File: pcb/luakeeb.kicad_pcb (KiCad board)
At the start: 2 copper layers, 138.9 x 95.2 mm, 123 parts, among them J1 Pimoroni, SW1 SW_Push, SW10 SW_Push, SW11 SW_Push, SW12 SW_Push, SW13 SW_Push, SW14 SW_Push, SW15 SW_Push, SW16 SW_Push, SW2 SW_Push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

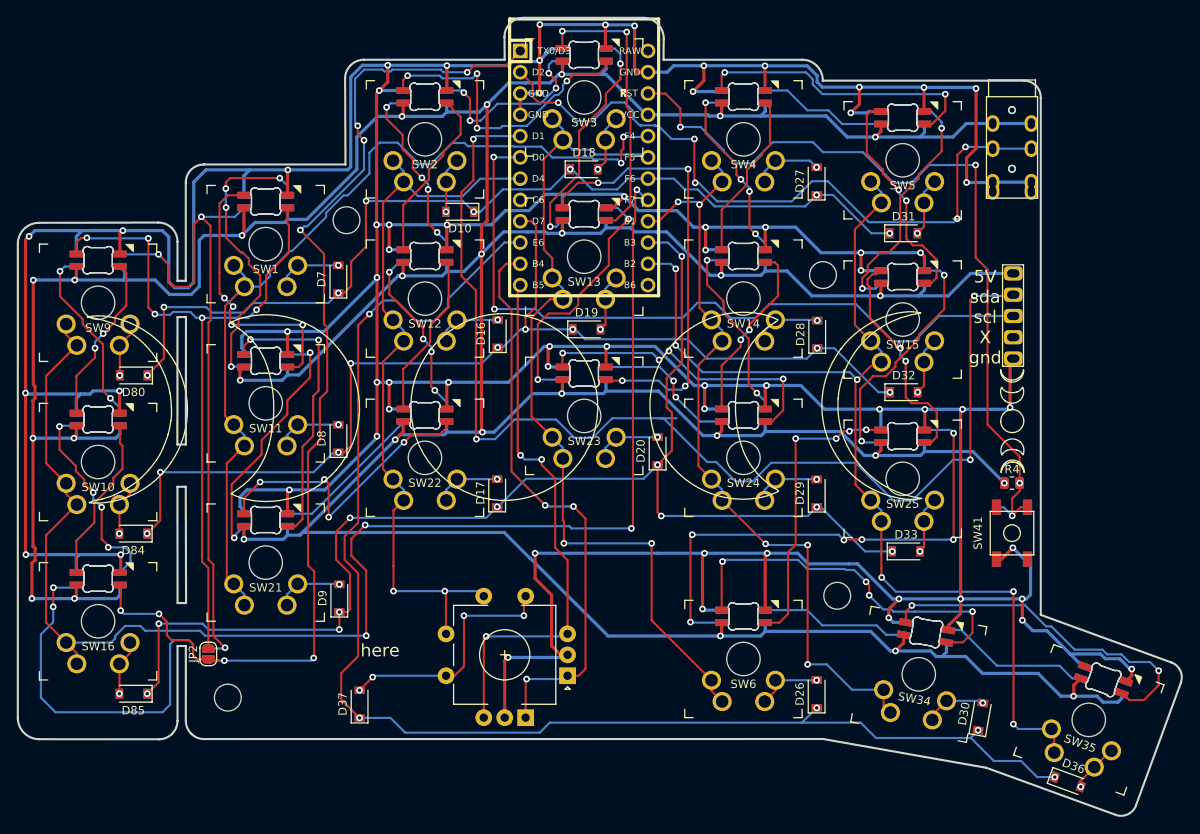
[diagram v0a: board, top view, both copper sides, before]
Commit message: removed the need for separate firmware per half by updating the footprint for the MX switch
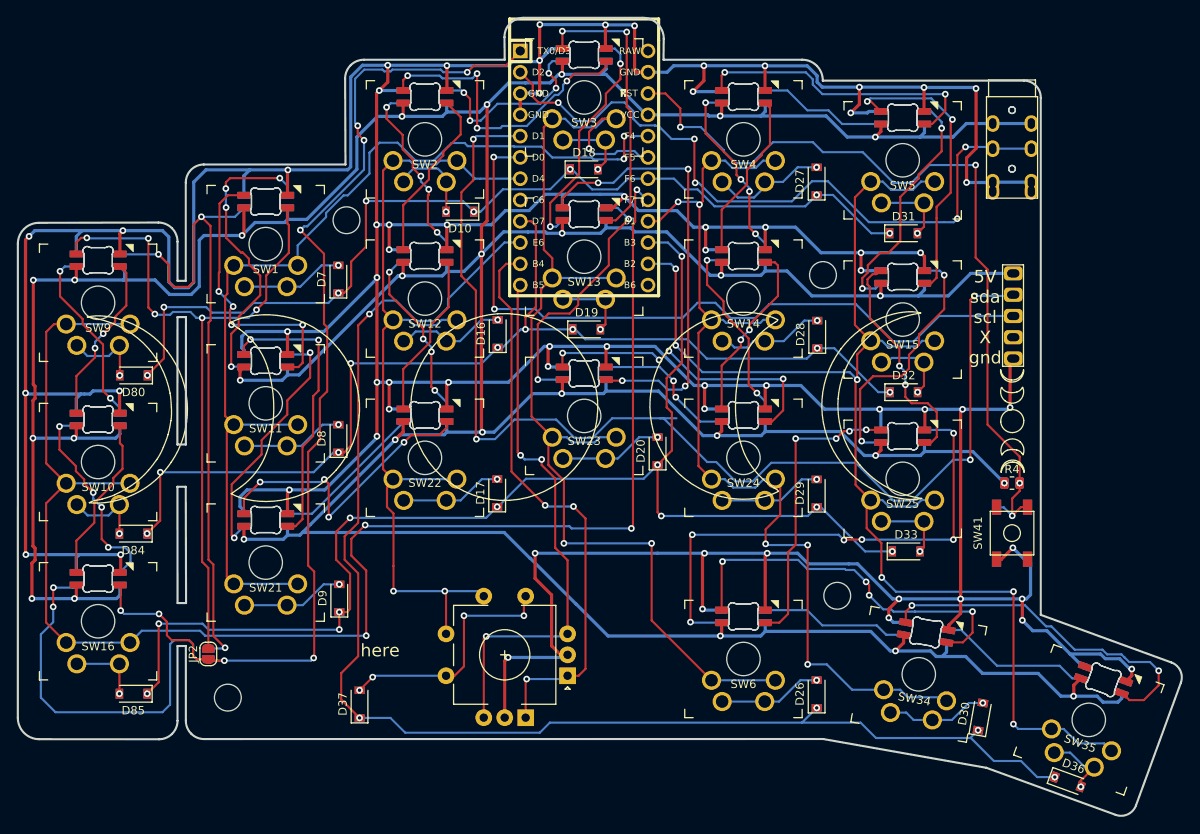
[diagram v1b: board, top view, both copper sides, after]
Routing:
- net col3: track 101.0 -> 129.8 mm, vias 2 -> 3
- net col5: track 129.5 -> 158.0 mm
- net col4: track 92.9 -> 118.9 mm
- net col2: track 88.4 -> 102.3 mm
- net col1: track 108.2 -> 118.7 mm
- net col0: track 173.5 -> 183.8 mm
- net Net-(D62-Pad2): track 27.1 -> 34.9 mm
- net Net-(D27-Pad2): track 8.31 -> 13.9 mm
- net Net-(D12-Pad2): track 7.94 -> 13.2 mm
- net Net-(D14-Pad2): track 8.10 -> 13.3 mm
- net Net-(D30-Pad2): track 7.43 -> 12.2 mm
- net Net-(D17-Pad2): track 7.87 -> 12.5 mm
- net Net-(D21-Pad2): track 8.06 -> 12.4 mm
- net Net-(D24-Pad2): track 8.01 -> 12.4 mm
- net Net-(D1-Pad2): track 7.93 -> 12.3 mm
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
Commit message: I actually don't know what changed, I must have forgotten to commit, whoops
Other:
- board text added: "luakeeb by sadekbaroudi, v2"

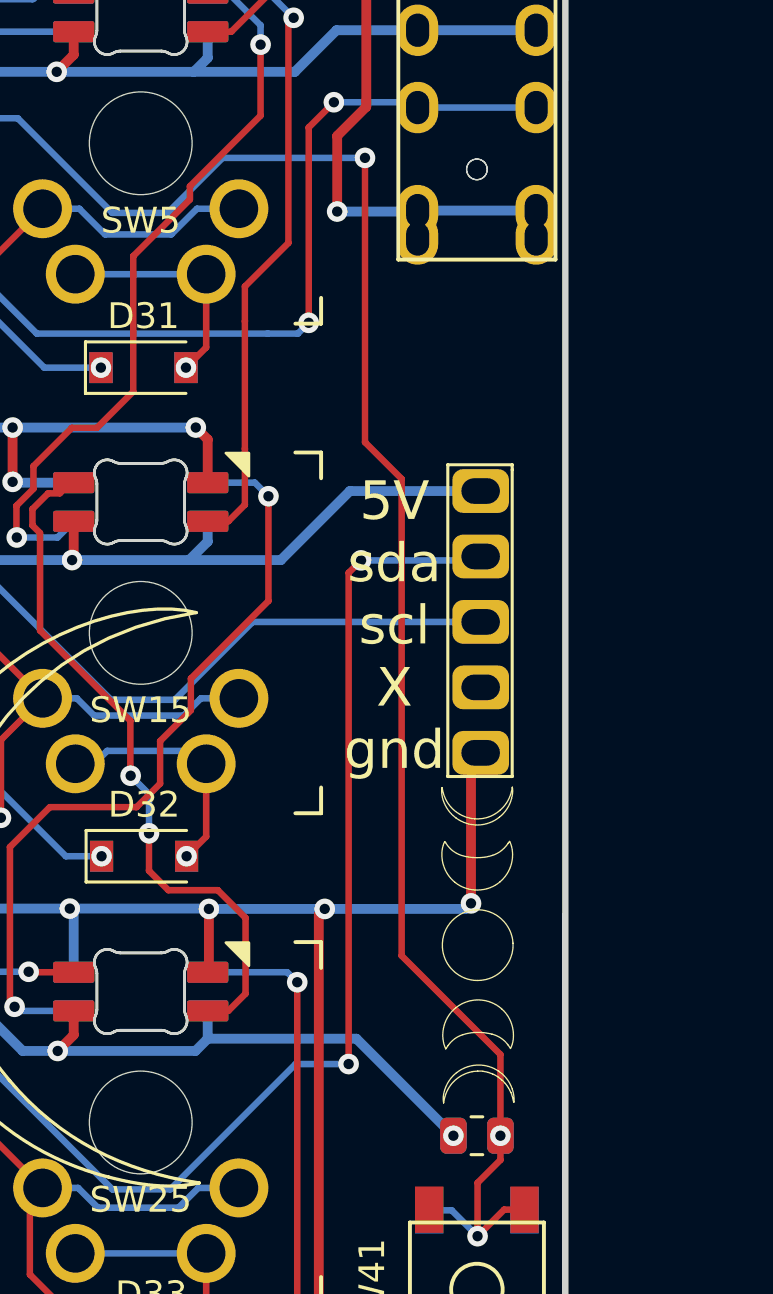
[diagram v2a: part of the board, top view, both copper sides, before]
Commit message: added support for the adafruit qwiic connector
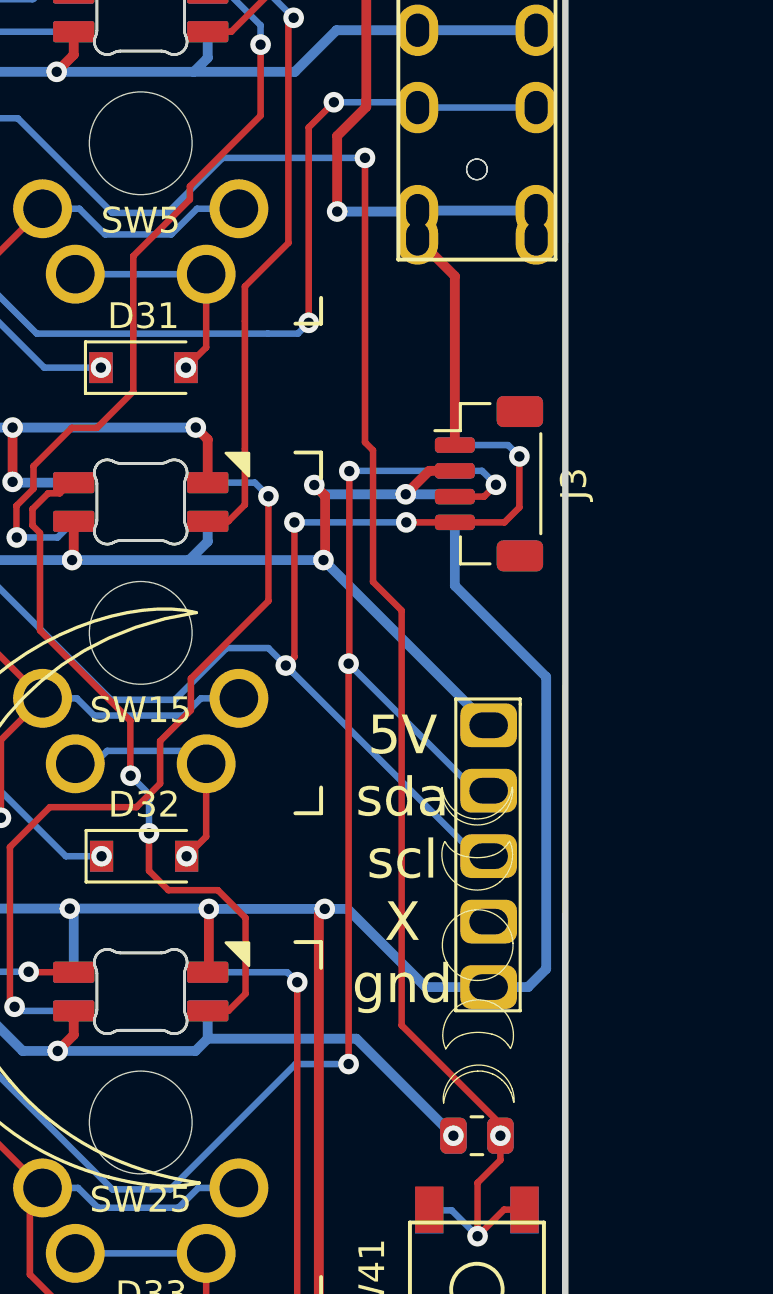
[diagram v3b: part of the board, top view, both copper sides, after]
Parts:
- added J2: Conn_01x04_Female, Connector_JST:JST_SH_BM04B-SRSS-TB_1x04-1MP_P1.00mm_Vertical, B.Cu at (150.5, 61.2)
- added J3: Conn_01x04_Female, Connector_JST:JST_SH_BM04B-SRSS-TB_1x04-1MP_P1.00mm_Vertical, F.Cu at (150.5, 61.2)
- moved J1 9.10 mm to (164.3, 75.7)
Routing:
- net GND: track 774.5 -> 800.2 mm, vias 64 -> 63
- net scl: track 89.0 -> 111.5 mm, vias 2 -> 6
- net sda: track 139.0 -> 152.8 mm, vias 4 -> 6
- net +5V: track 620.4 -> 633.3 mm, vias 28 -> 31

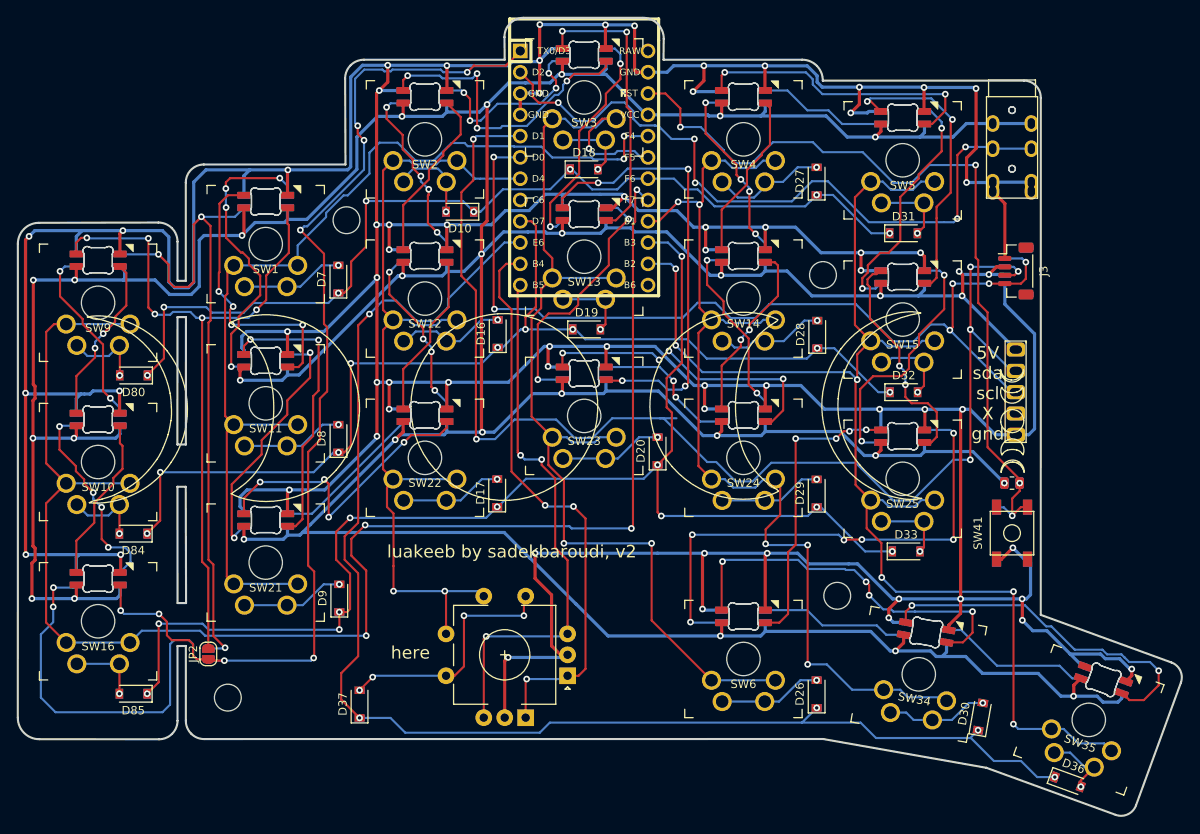
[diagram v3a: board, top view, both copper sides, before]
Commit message: added wireless support for nice nano with wiring, jst connector, and on off switch
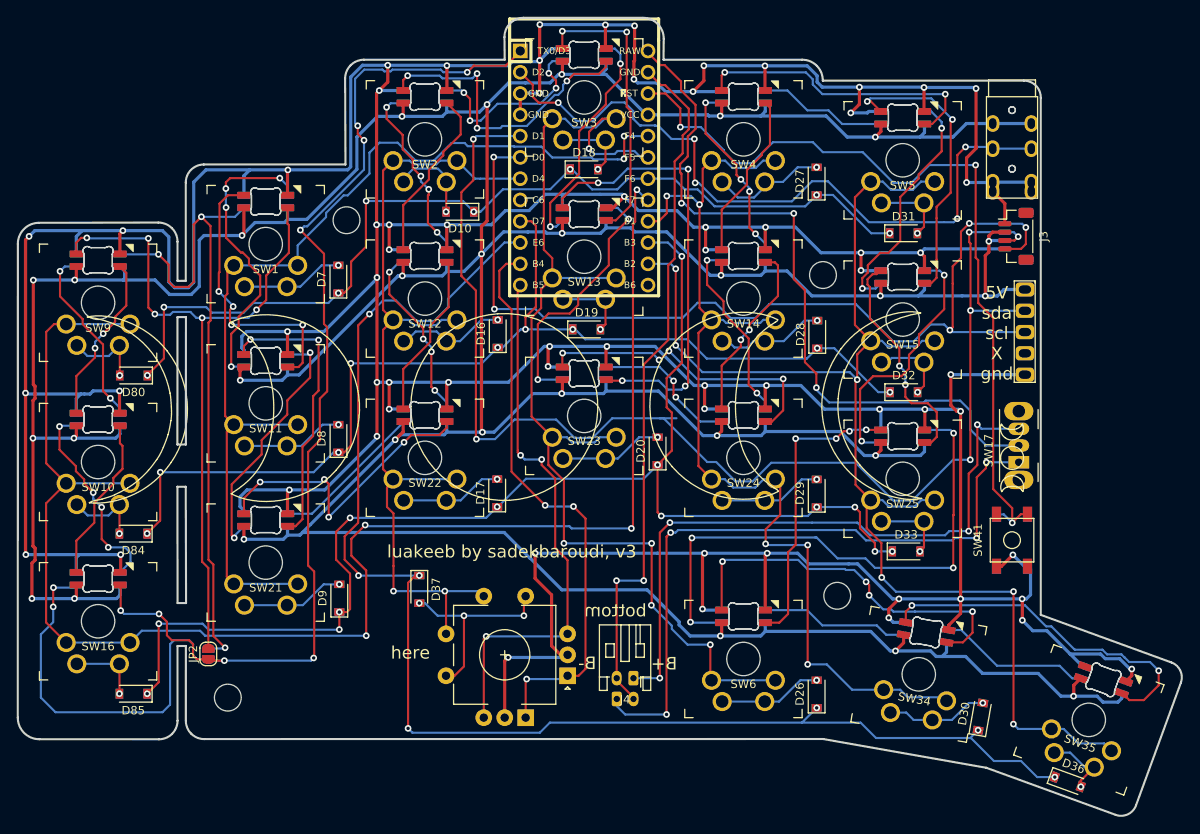
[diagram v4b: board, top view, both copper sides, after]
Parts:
- removed R1, R4: 10k, Resistor_SMD:R_0805_2012Metric
- added J4: Conn_01x02_Female, Connector_JST:JST_PH_S2B-PH-K_1x02_P2.00mm_Horizontal, F.Cu at (104.9, 109.8)
- added J5: Conn_01x02_Female, Connector_JST:JST_PH_S2B-PH-K_1x02_P2.00mm_Horizontal, B.Cu at (102.9, 112.3)
- added SW17: SW_DPDT_x2, Button_Switch_THT:SW_CuK_OS102011MA1QN1_SPDT_Angled, F.Cu at (150.9, 84.1)
- moved D37 15.4 mm to (79.3, 99.2), turned to 270 degrees
- moved D81 15.4 mm to (79.3, 99.2), turned to 270 degrees
- moved J1 7.25 mm to (165.4, 68.5)
- moved J2 4.14 mm to (150.5, 57.1)
- moved J3 4.14 mm to (150.5, 57.1)
- moved SW41 0.84 mm to (150.0, 93.3)
- moved SW8 0.84 mm to (150.0, 93.4)
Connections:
- U1 pad 23: GND -> B-
- U1 pad 24: Net-(U1-Pad24) -> B+
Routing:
- net B+: track 0.00 -> 86.1 mm, vias 0 -> 3
- net B-: track 0.00 -> 83.4 mm, vias 0 -> 2
- net Net-(J5-Pad1): track 0.00 -> 79.8 mm, vias 0 -> 4
- net Net-(J4-Pad1): track 0.00 -> 77.0 mm, vias 0 -> 4
- net +5V: track 633.3 -> 621.5 mm, vias 31 -> 29
- net GND: track 800.2 -> 790.2 mm, vias 63 -> 65
- net Net-(D37-Pad2): track 29.3 -> 24.2 mm, vias 4 -> 3
- net Net-(D56-Pad2): track 62.1 -> 66.3 mm, vias 6 -> 4
- net scl: track 111.5 -> 115.7 mm, vias 6 -> 5
- net sda: track 152.8 -> 156.2 mm
- net col4: track 118.9 -> 120.6 mm
- net row2: track 153.7 -> 155.4 mm, vias 11 -> 13
- net col3: track 129.8 -> 131.4 mm, vias 3 -> 5
- net row3: track 166.6 -> 167.9 mm, vias 5 -> 7
- net RESET: track 96.8 -> 96.9 mm, vias 4 -> 3
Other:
- board text added: "B+"
- board text added: "B-"
- board text added: "bottom"
- board text added: "luakeeb by sadekbaroudi, v3"
- board text removed: "luakeeb by sadekbaroudi, v2"
